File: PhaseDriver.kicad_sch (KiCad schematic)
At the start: 38 parts

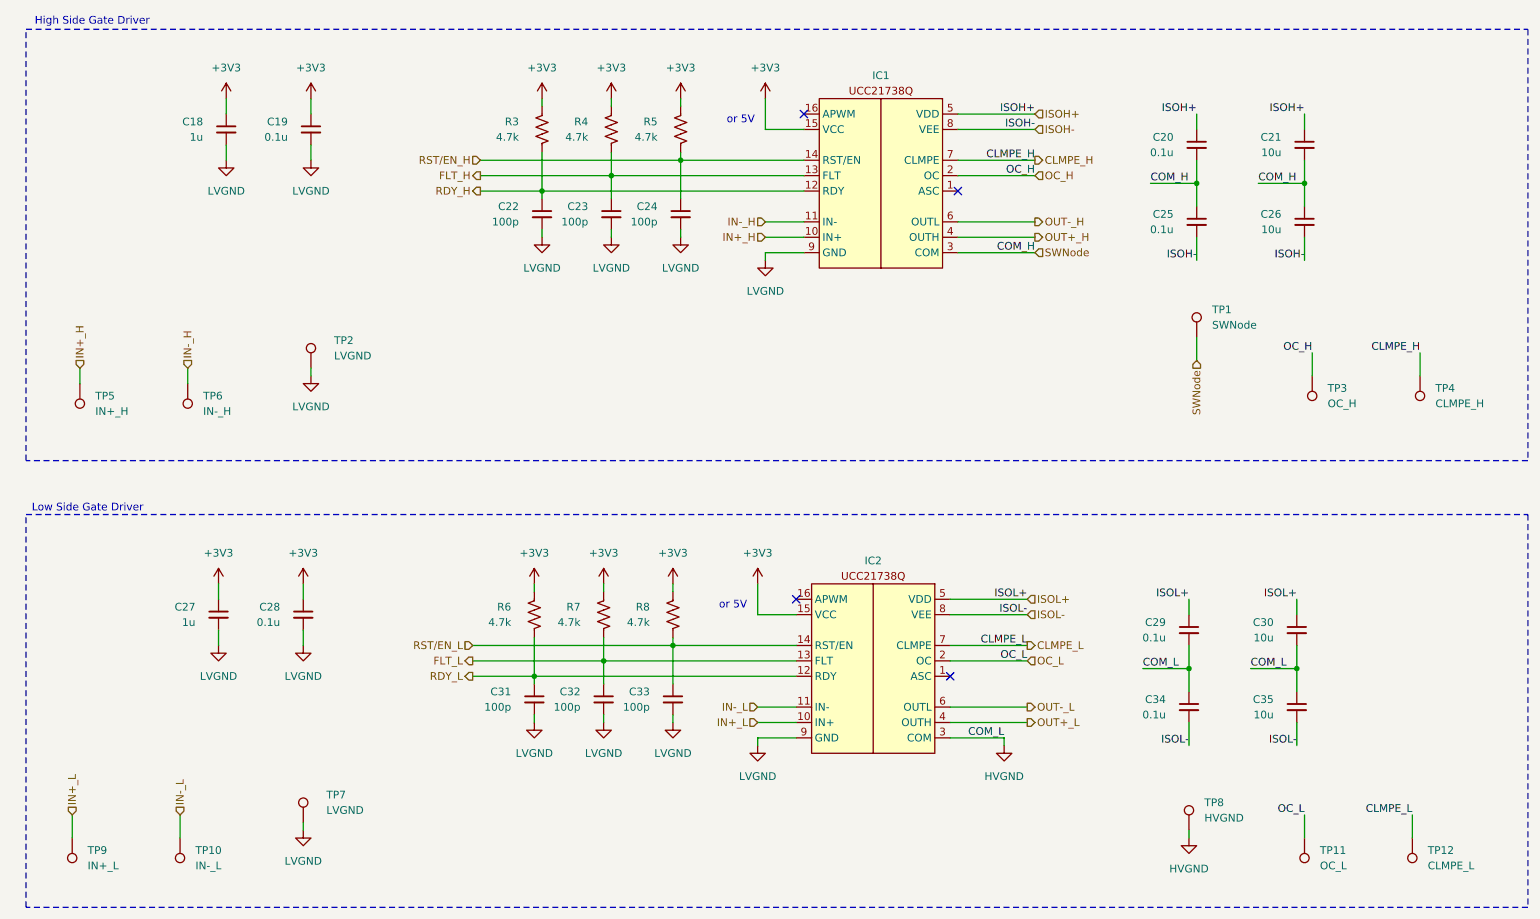
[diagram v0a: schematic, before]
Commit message: new bulk caps, new HV+,- connector placement
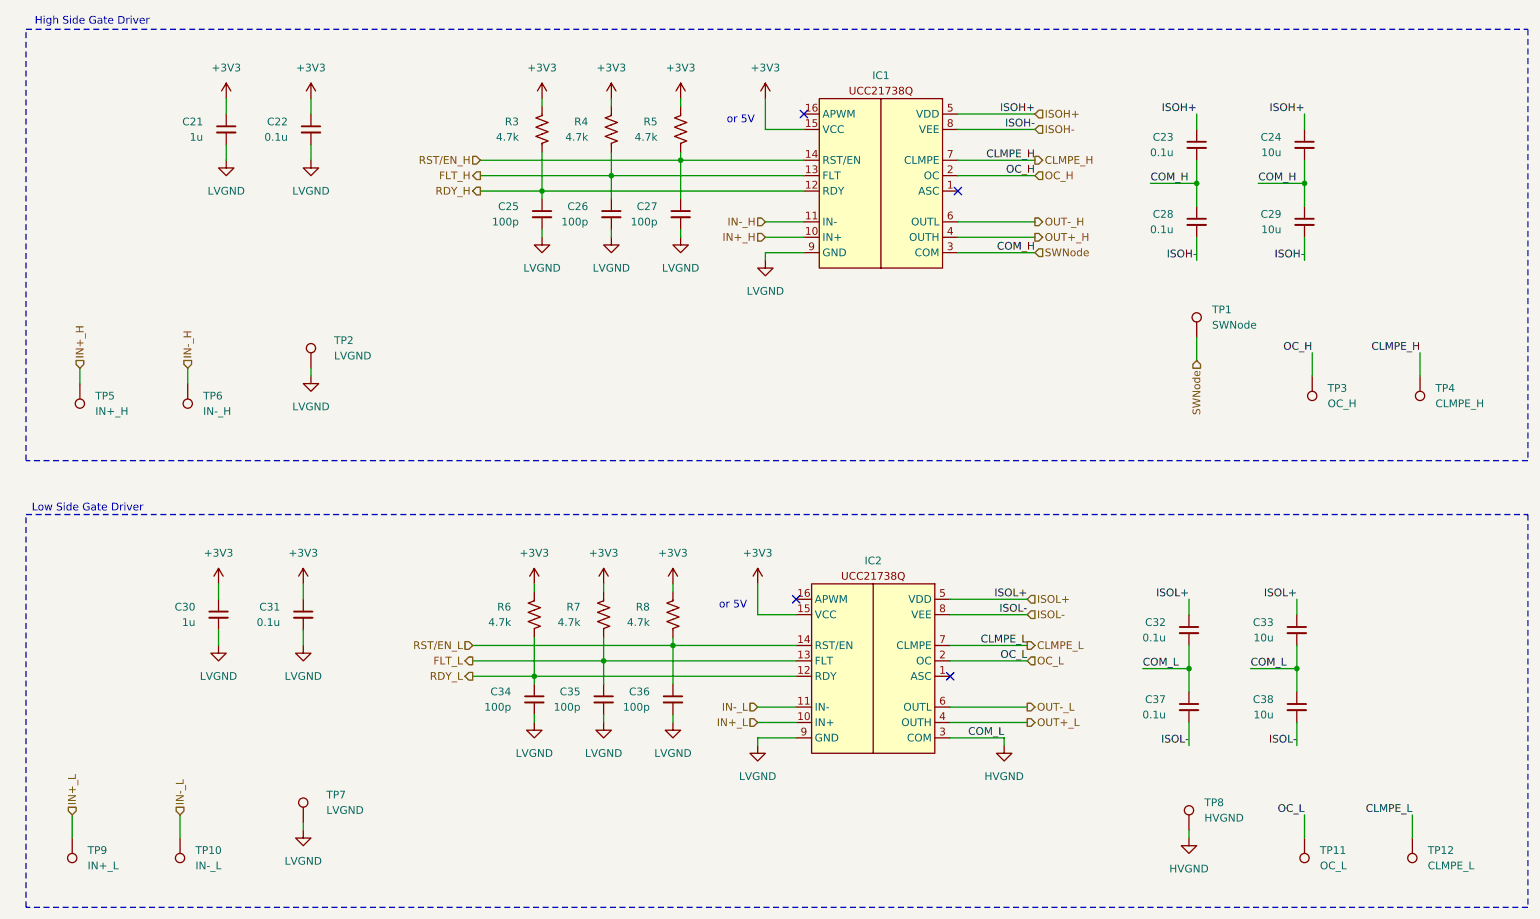
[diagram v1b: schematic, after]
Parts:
- renumbered C18 to C21, C19 to C22, C20 to C23, C21 to C24, C22 to C25, C23 to C26, C24 to C27, C25 to C28, C26 to C29, C27 to C30, C28 to C31, C29 to C32, C30 to C33, C31 to C34, C32 to C35, C33 to C36, C34 to C37, C35 to C38

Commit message: killed testpoints
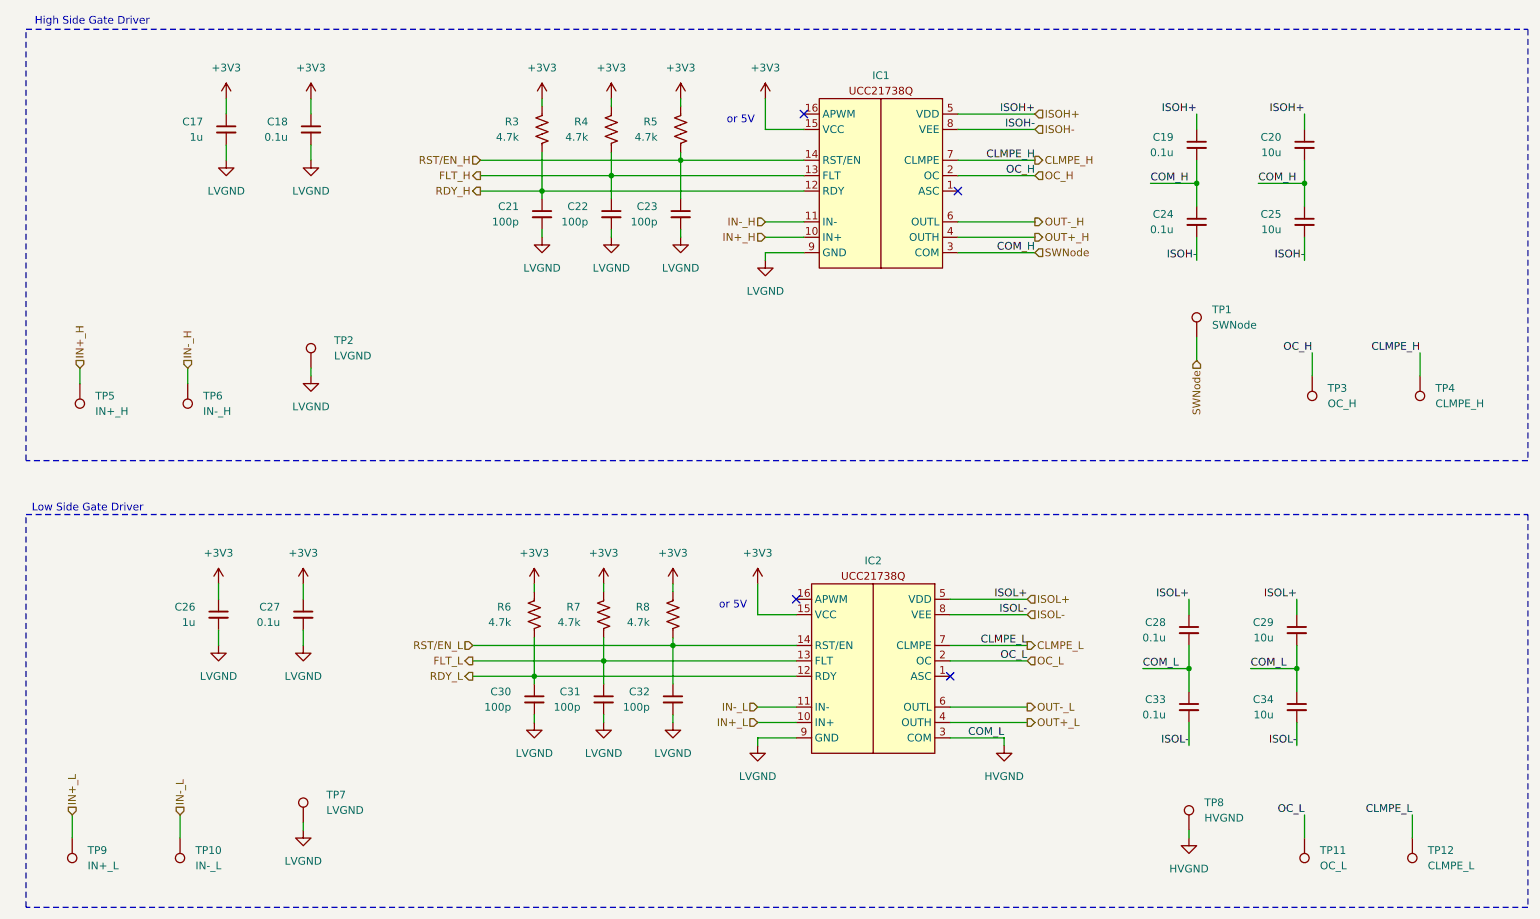
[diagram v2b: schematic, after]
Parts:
- renumbered C21 to C17, C22 to C18, C23 to C19, C24 to C20, C25 to C21, C26 to C22, C27 to C23, C28 to C24, C29 to C25, C30 to C26, C31 to C27, C32 to C28, C33 to C29, C34 to C30, C35 to C31, C36 to C32, C37 to C33, C38 to C34

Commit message: testpoints and silkscreen
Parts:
- TP11, TP3: footprint TractionInverter:KEYSTONE_5281 -> TestPoint:TestPoint_Pad_D1.5mm
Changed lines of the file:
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@@
 			)
 		)
-		(property "Footprint" "TractionInverter:KEYSTONE_5281"
+		(property "Footprint" "TestPoint:TestPoint_Pad_D1.5mm"
 			(at 236.22 151.13 0)
 			(effects
@@
 			)
 		)
-		(property "Footprint" "TractionInverter:KEYSTONE_5281"
+		(property "Footprint" "TestPoint:TestPoint_Pad_D1.5mm"
 			(at 237.49 74.93 0)
 			(effects
